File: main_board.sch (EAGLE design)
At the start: 43 parts, among them P1 ST-TF-003A, U1 STM32F407VGT6, U2 USBLC6-2, U3 MCP1700T-3302E, U4 LTC4054LES5-4.2#TRPBF, X1 MicroUSB-B

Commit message: schematics in progress..
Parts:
- added JP4: LCD, pinhead:PINHD-1X14
- added R8: 1k, rcl:R-EU_R0805
- added S2: INT-1500M90B, int-1500m90b:SMD-BUTTON(6P-10X10X8.6MM)-SKQUDBE010
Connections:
- net PB5 renamed NCHRG
- new net LCD_CS: JP4.3, U1G$2.PC4
- new net LCD_DC: JP4.5, U1G$2.PC5
- new net LCD_MISO: JP4.9, U1G$1.PA6
- new net LCD_MOSI: JP4.6, U1G$1.PA7
- new net LCD_SCK: JP4.7, U1G$1.PA5
- new net N$17: S2.1, U1G$1.PA0
- new net N$19: S2.2, U1G$1.PA1
- new net N$20: S2.3, U1G$1.PA2
- new net N$21: S2.5, U1G$1.PA3
- new net N$22: S2.6, U1G$1.PA4
- new net N$23: R8.1, S2.4
- net +3V3: now also JP4.1, JP4.8, R8.2
- net GND: now also JP4.10, JP4.11, JP4.12, JP4.13, JP4.14, JP4.2
- net NRST: now also JP4.4
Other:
- moved on the sheet: C1, C14, C15, C17, C18, C19, C2, C20, C21, C3, C4, C5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

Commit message: pcb in progress..
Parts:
- removed C14: 100n, rcl:C-EUC0805
- removed C15: 1u, rcl:C-EUC0805
- removed R4: 47, rcl:R-EU_R0805
- added C22: 100n, rcl:C-EUC0805
- added R10: 20k, rcl:R-EU_R0805
- added R9: 10k, rcl:R-EU_R0805
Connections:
- net N$12 renamed PROG
- net N$13 renamed SD_DAT3
- net N$14 renamed SD_CLK
- net N$15 renamed SD_DAT0
- net N$16 renamed SD_DAT1
- net N$18 renamed SD_CMD
- net N$23 renamed BTN_COM
- net N$4 renamed SD_DAT2
- removed net +3V3: JP4.1, JP4.8, P1.VDD, R8.2
- removed net N$17: S2.1, U1G$1.PA0
- removed net N$19: S2.2, U1G$1.PA1
- removed net N$20: S2.3, U1G$1.PA2
- removed net N$21: S2.5, U1G$1.PA3
- removed net N$22: S2.6, U1G$1.PA4
- removed net VREF+: C14.1, C15.1, R4.2, U1G$3.VREF+
- new net BTN_0: S2.6, U1G$1.PB4
- new net BTN_1: S2.1, U1G$1.PB3
- new net BTN_2: S2.5, U1G$2.PD7
- new net BTN_3: S2.3, U1G$2.PD6
- new net BTN_4: S2.2, U1G$2.PD5
- new net VBUS: R10.2, R9.1, U1G$1.PA9
- net +5V: now also R9.2, U2.GND; no longer U2.VBUS
- net D+: now also U2.I/O1B; no longer U2.I/O1
- net D+_PROT: now also U2.I/O1; no longer U2.I/O1B
- net D-: now also U2.I/O2B; no longer U2.I/O2
- net D-_INT: now also U2.I/O2; no longer U2.I/O2B
- net GND: now also C22.2, R10.1, U2.VBUS; no longer C14.2, C15.2, U2.GND
- net VDD: now also C22.1, JP4.1, JP4.8, P1.VDD, R8.2
- net VDDA: now also U1G$3.VREF+; no longer R4.1
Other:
- moved on the sheet: C17, C18, R8, S2

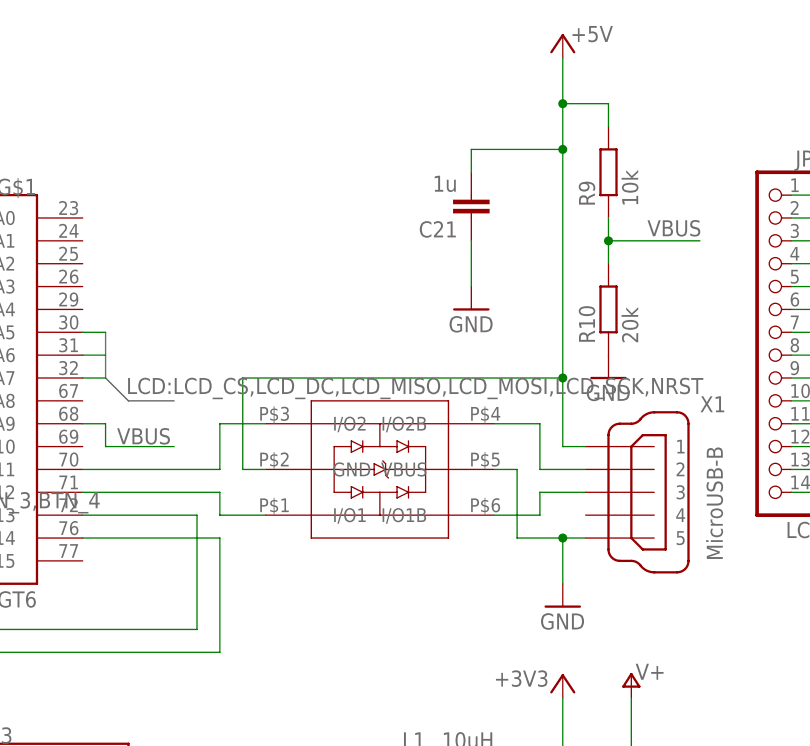
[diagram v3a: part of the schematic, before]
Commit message: fix scheme error
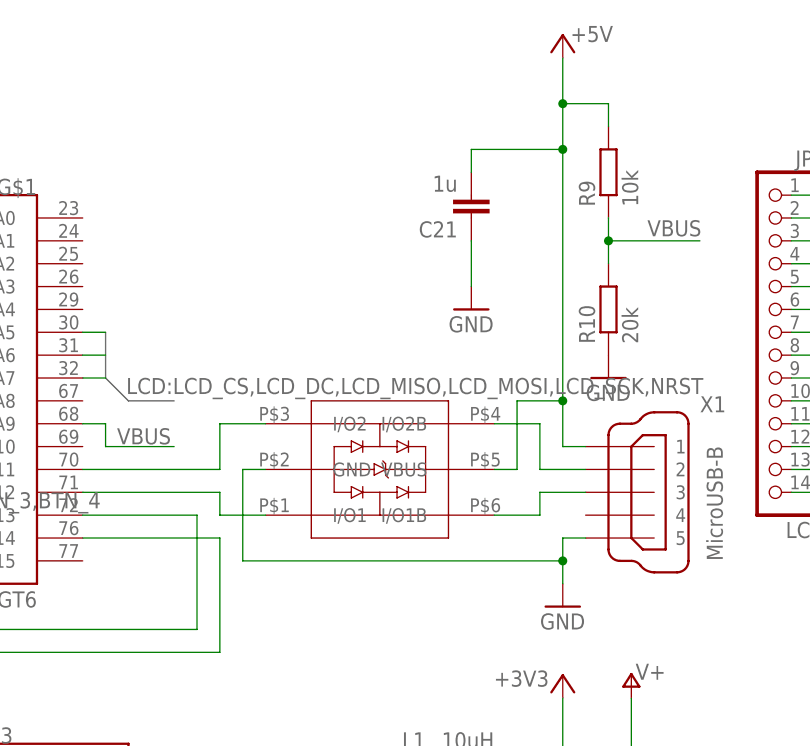
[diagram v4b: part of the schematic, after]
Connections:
- net +5V: now also U2.VBUS; no longer U2.GND
- net GND: now also U2.GND; no longer U2.VBUS
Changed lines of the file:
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@@
 <wire x1="58.42" y1="55.88" x2="55.88" y2="55.88" width="0.1524" layer="91"/>
 <pinref part="GND4" gate="1" pin="GND"/>
-<wire x1="55.88" y1="55.88" x2="55.88" y2="50.8" width="0.1524" layer="91"/>
-<wire x1="50.8" y1="63.5" x2="50.8" y2="55.88" width="0.1524" layer="91"/>
-<wire x1="50.8" y1="55.88" x2="55.88" y2="55.88" width="0.1524" layer="91"/>
-<junction x="55.88" y="55.88"/>
-<pinref part="U2" gate="G$1" pin="VBUS"/>
-<wire x1="48.26" y1="63.5" x2="50.8" y2="63.5" width="0.1524" layer="91"/>
+<wire x1="55.88" y1="55.88" x2="55.88" y2="53.34" width="0.1524" layer="91"/>
+<pinref part="U2" gate="G$1" pin="GND"/>
+<wire x1="55.88" y1="53.34" x2="55.88" y2="50.8" width="0.1524" layer="91"/>
+<wire x1="22.86" y1="63.5" x2="20.32" y2="63.5" width="0.1524" layer="91"/>
+<wire x1="20.32" y1="63.5" x2="20.32" y2="53.34" width="0.1524" layer="91"/>
+<wire x1="20.32" y1="53.34" x2="55.88" y2="53.34" width="0.1524" layer="91"/>
+<junction x="55.88" y="53.34"/>
 </segment>
 <segment>
@@
 <wire x1="55.88" y1="109.22" x2="55.88" y2="104.14" width="0.1524" layer="91"/>
 <wire x1="55.88" y1="104.14" x2="55.88" y2="99.06" width="0.1524" layer="91"/>
-<wire x1="55.88" y1="99.06" x2="55.88" y2="73.66" width="0.1524" layer="91"/>
-<wire x1="55.88" y1="73.66" x2="55.88" y2="66.04" width="0.1524" layer="91"/>
+<wire x1="55.88" y1="99.06" x2="55.88" y2="71.12" width="0.1524" layer="91"/>
+<wire x1="55.88" y1="71.12" x2="55.88" y2="66.04" width="0.1524" layer="91"/>
 <wire x1="55.88" y1="66.04" x2="58.42" y2="66.04" width="0.1524" layer="91"/>
 <pinref part="X1" gate="G$1" pin="1"/>
-<wire x1="20.32" y1="63.5" x2="20.32" y2="73.66" width="0.1524" layer="91"/>
-<wire x1="20.32" y1="73.66" x2="55.88" y2="73.66" width="0.1524" layer="91"/>
-<junction x="55.88" y="73.66"/>
 <pinref part="C21" gate="G$1" pin="2"/>
 <wire x1="45.72" y1="96.52" x2="45.72" y2="99.06" width="0.1524" layer="91"/>
@@
 <wire x1="60.96" y1="104.14" x2="55.88" y2="104.14" width="0.1524" layer="91"/>
 <junction x="55.88" y="104.14"/>
-<pinref part="U2" gate="G$1" pin="GND"/>
-<wire x1="22.86" y1="63.5" x2="20.32" y2="63.5" width="0.1524" layer="91"/>
-</segment>
-<segment>
+<pinref part="U2" gate="G$1" pin="VBUS"/>
+<wire x1="48.26" y1="63.5" x2="50.8" y2="63.5" width="0.1524" layer="91"/>
+<wire x1="50.8" y1="63.5" x2="50.8" y2="71.12" width="0.1524" layer="91"/>
+<wire x1="50.8" y1="71.12" x2="55.88" y2="71.12" width="0.1524" layer="91"/>
+<junction x="55.88" y="71.12"/>
+</segment>
+<segment>
